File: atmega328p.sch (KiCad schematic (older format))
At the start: 6 parts, among them J6 ICSP, U6 ATMEGA328PB-AU, Y1 CSTNE16M0VH3L000R0

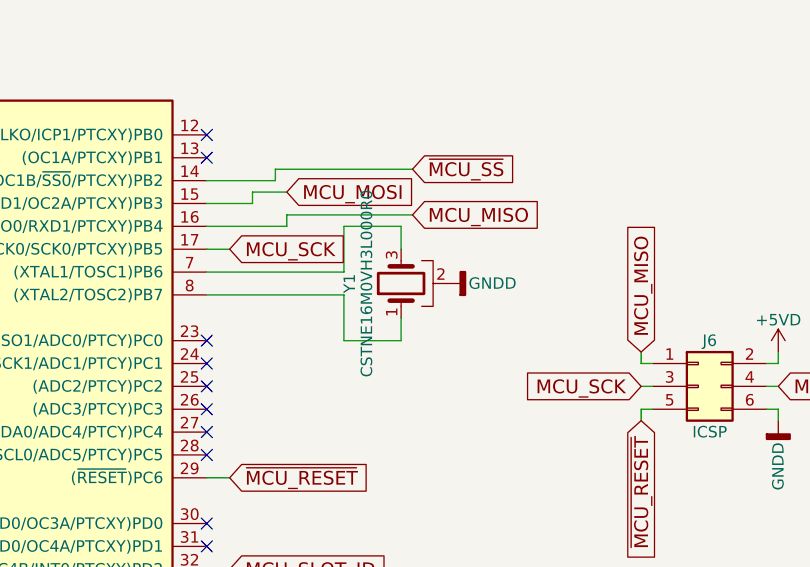
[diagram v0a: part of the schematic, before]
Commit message: Add onboard ATMEGA328PB
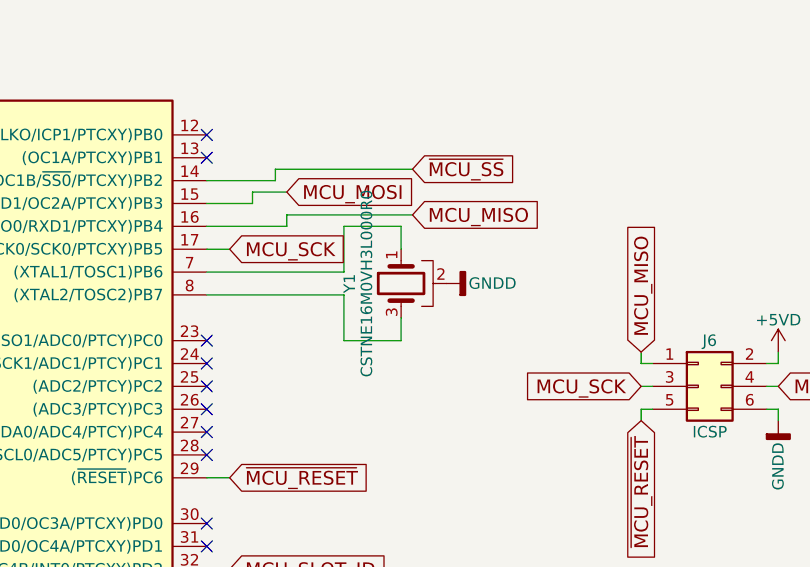
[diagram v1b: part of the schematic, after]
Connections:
- net at U6.7 ((XTAL1/TOSC1)PB6): now also Y1.1; no longer Y1.3
- net at U6.8 ((XTAL2/TOSC2)PB7): now also Y1.3; no longer Y1.1
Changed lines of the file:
@@
 F 3 "" H 7300 2950 50  0001 C CNN
 	1    7300 2950
-	0    -1   -1   0
+	0    -1   1    0
 $EndComp
 Wire Wire Line

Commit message: Fixed the THS7374 filter stuff, moved to Kicad 5
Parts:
- C15, C16, C17: symbol C -> bkm-129x-simple-rescue:C
- J6: symbol Conn_02x03_Odd_Even -> bkm-129x-simple-rescue:Conn_02x03_Odd_Even
- U6: symbol ATMEGA328PB-AU -> bkm-129x-simple-rescue:ATMEGA328PB-AU
- Y1: symbol Crystal_GND2 -> bkm-129x-simple-rescue:Crystal_GND2
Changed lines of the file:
@@
-EESchema Schematic File Version 2
-LIBS:power
-LIBS:device
-LIBS:switches
-LIBS:relays
-LIBS:motors
-LIBS:transistors
-LIBS:conn
-LIBS:linear
-LIBS:regul
-LIBS:74xx
-LIBS:cmos4000
-LIBS:adc-dac
-LIBS:memory
-LIBS:xilinx
-LIBS:microcontrollers
-LIBS:dsp
-LIBS:microchip
-LIBS:analog_switches
-LIBS:motorola
-LIBS:texas
-LIBS:intel
-LIBS:audio
-LIBS:interface
-LIBS:digital-audio
-LIBS:philips
-LIBS:display
-LIBS:cypress
-LIBS:siliconi
-LIBS:opto
-LIBS:atmel
-LIBS:contrib
-LIBS:valves
-LIBS:ths7374
-LIBS:arduino-nano-v3
-LIBS:adg734
-LIBS:adg1611
-LIBS:dtc144eka
-LIBS:mic3490
-LIBS:bkm-129x-simple-cache
-EELAYER 25 0
+EESchema Schematic File Version 4
+EELAYER 30 0
 EELAYER END
 $Descr A4 11693 8268
@@
 $EndDescr
 $Comp
-L ATMEGA328PB-AU U6
+L bkm-129x-simple-rescue:ATMEGA328PB-AU U6
 U 1 1 5F1F180C
 P 5150 3500
@@
 $EndComp
 $Comp
-L Crystal_GND2 Y1
+L bkm-129x-simple-rescue:Crystal_GND2 Y1
 U 1 1 5F1F1898
 P 7300 2950
@@
 	7300 3200 7300 3100
 $Comp
-L GNDD #PWR062
+L power:GNDD #PWR062
 U 1 1 5F1F1A3C
 P 7500 2950
@@
 	6450 3800 6550 3800
 $Comp
-L GNDD #PWR063
+L power:GNDD #PWR063
 U 1 1 5F1F5487
 P 5000 5100
@@
 NoConn ~ 3850 4400
 $Comp
-L C C16
+L bkm-129x-simple-rescue:C C16
 U 1 1 5F1F6C18
 P 4650 1650
@@
 $EndComp
 $Comp
-L C C15
+L bkm-129x-simple-rescue:C C15
 U 1 1 5F1F6C65
 P 4400 1650
@@
 $EndComp
 $Comp
-L +5VD #PWR064
+L power:+5VD #PWR064
 U 1 1 5F1F6CE5
 P 4400 1400
@@
 	5050 1450 5050 2000
 $Comp
-L C C17
+L bkm-129x-simple-rescue:C C17
 U 1 1 5F1F6E50
 P 3600 2600
@@
 $EndComp
 $Comp
-L GNDD #PWR065
+L power:GNDD #PWR065
 U 1 1 5F1F6EA7
 P 3350 2600
@@
 Connection ~ 4400 1850
 $Comp
-L GNDD #PWR066
+L power:GNDD #PWR066
 U 1 1 5F1F802F
 P 4400 1850
@@
 NoConn ~ 3850 4200
 $Comp
-L Conn_02x03_Odd_Even J6
+L bkm-129x-simple-rescue:Conn_02x03_Odd_Even J6
 U 1 1 5F1FE23D
 P 8600 3400
@@
 $EndComp
 $Comp
-L GNDD #PWR067
+L power:GNDD #PWR067
 U 1 1 5F1FE2BE
 P 8950 3550
@@
 $EndComp
 $Comp
-L +5VD #PWR068
+L power:+5VD #PWR068
 U 1 1 5F1FE30F
 P 8950 3250

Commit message: Revision D
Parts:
- C15, C16, C17: footprint Capacitors_SMD:C_0805_HandSoldering -> Capacitor_SMD:C_0805_2012Metric_Pad1.18x1.45mm_HandSolder
- U6: footprint Housings_QFP:TQFP-32_7x7mm_Pitch0.8mm -> Package_QFP:TQFP-32_7x7mm_P0.8mm
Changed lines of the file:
@@
 F 0 "U6" H 4750 4975 50  0000 R BNN
 F 1 "ATMEGA328PB-AU" H 4750 4900 50  0000 R BNN
-F 2 "Housings_QFP:TQFP-32_7x7mm_Pitch0.8mm" H 5100 2100 50  0001 L CIN
+F 2 "Package_QFP:TQFP-32_7x7mm_P0.8mm" H 5100 2100 50  0001 L CIN
 F 3 "" H 4850 3550 50  0001 C CNN
 	1    5150 3500
@@
 	4950 5000 4950 5050
 Wire Wire Line
-	4950 5050 5050 5050
+	4950 5050 5000 5050
 Wire Wire Line
 	5000 5050 5000 5100
@@
 F 0 "C16" H 4675 1750 50  0000 L CNN
 F 1 "4.7uF" H 4675 1550 50  0000 L CNN
-F 2 "Capacitors_SMD:C_0805_HandSoldering" H 4688 1500 50  0001 C CNN
+F 2 "Capacitor_SMD:C_0805_2012Metric_Pad1.18x1.45mm_HandSolder" H 4688 1500 50  0001 C CNN
 F 3 "" H 4650 1650 50  0001 C CNN
 	1    4650 1650
@@
 F 0 "C15" H 4425 1750 50  0000 L CNN
 F 1 "1uF" H 4425 1550 50  0000 L CNN
-F 2 "Capacitors_SMD:C_0805_HandSoldering" H 4438 1500 50  0001 C CNN
+F 2 "Capacitor_SMD:C_0805_2012Metric_Pad1.18x1.45mm_HandSolder" H 4438 1500 50  0001 C CNN
 F 3 "" H 4400 1650 50  0001 C CNN
 	1    4400 1650
@@
 $EndComp
 Wire Wire Line
-	4400 1400 4400 1500
+	4400 1400 4400 1450
 Wire Wire Line
 	4650 1450 4650 1500
@@
 	4850 1900 5050 1900
 Wire Wire Line
-	5050 1450 5050 2000
+	5050 1450 5050 1900
 $Comp
 L bkm-129x-simple-rescue:C C17
@@
 F 0 "C17" H 3625 2700 50  0000 L CNN
 F 1 "100nF" H 3625 2500 50  0000 L CNN
-F 2 "Capacitors_SMD:C_0805_HandSoldering" H 3638 2450 50  0001 C CNN
+F 2 "Capacitor_SMD:C_0805_2012Metric_Pad1.18x1.45mm_HandSolder" H 3638 2450 50  0001 C CNN
 F 3 "" H 3600 2600 50  0001 C CNN
 	1    3600 2600
@@
 	4400 1850 4650 1850
 Wire Wire Line
-	4400 1450 5050 1450
+	4400 1450 4650 1450
+Wire Wire Line
+	5000 5050 5050 5050
+Wire Wire Line
+	4400 1450 4400 1500
+Wire Wire Line
+	5050 1900 5050 2000
+Wire Wire Line
+	4650 1450 5050 1450
 $EndSCHEMATC
